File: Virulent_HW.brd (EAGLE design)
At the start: 52 parts, among them U1 STM32F050G6U6

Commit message: updated LED symbol
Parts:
- RGB1: value MSL0201RGBW15 -> MSL0201RGBLED
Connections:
- net +3.3V: now also RGB1.4; no longer RGB1.P$4
- net MOD_FREQ: now also U1.9
- net N$11: now also RGB1.1; no longer RGB1.P$1
- net N$15: now also RGB1.2; no longer RGB1.P$2
- net N$16: now also RGB1.3; no longer RGB1.P$3
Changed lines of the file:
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@@
 <element name="R9" library="Virulent_HW" package="R0402" value="10k" x="-33.02" y="-237.49"/>
 <element name="R10" library="Virulent_HW" package="R0402" value="10k" x="-33.02" y="-242.57"/>
-<element name="RGB1" library="Virulent_HW" package="MSL0201RGB" value="MSL0201RGBW15" x="-39.37" y="-241.3"/>
+<element name="RGB1" library="Virulent_HW" package="MSL0201RGB" value="MSL0201RGBLED" x="-39.37" y="-241.3"/>
 <element name="R11" library="Virulent_HW" package="R0402" value="10k" x="-40.64" y="-247.65"/>
 <element name="R12" library="Virulent_HW" package="R0402" value="10k" x="-40.64" y="-252.73"/>
@@
 <contactref element="R8" pad="2"/>
 <contactref element="R10" pad="2"/>
-<contactref element="RGB1" pad="P$4"/>
+<contactref element="RGB1" pad="4"/>
 <contactref element="R14" pad="2"/>
 <contactref element="R16" pad="2"/>
@@
 </signal>
 <signal name="N$11">
-<contactref element="RGB1" pad="P$1"/>
+<contactref element="RGB1" pad="1"/>
 <contactref element="R11" pad="1"/>
 <wire x1="-39.445" y1="-242.75" x2="-41.29" y2="-247.65" width="0" layer="19" extent="1-1"/>
 </signal>
 <signal name="N$15">
-<contactref element="RGB1" pad="P$2"/>
+<contactref element="RGB1" pad="2"/>
 <contactref element="R12" pad="1"/>
 <wire x1="-39.045" y1="-241.7" x2="-41.29" y2="-252.73" width="0" layer="19" extent="1-1"/>
 </signal>
 <signal name="N$16">
-<contactref element="RGB1" pad="P$3"/>
+<contactref element="RGB1" pad="3"/>
 <contactref element="R13" pad="1"/>
 <wire x1="-39.045" y1="-240.9" x2="-41.29" y2="-257.81" width="0" layer="19" extent="1-1"/>
@@
 <signal name="MOD_FREQ">
 <contactref element="SPST1" pad="4"/>
+<contactref element="U1" pad="9"/>
+<wire x1="-37.15" y1="-285.13" x2="-34.02" y2="-216.505" width="0" layer="19" extent="1-1"/>
 </signal>
 <signal name="N$26">

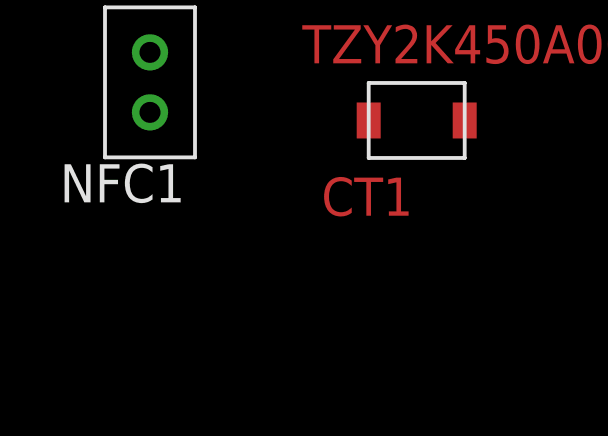
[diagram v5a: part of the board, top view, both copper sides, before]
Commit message: added no place capcitor to NFC coil transmitter in case needed
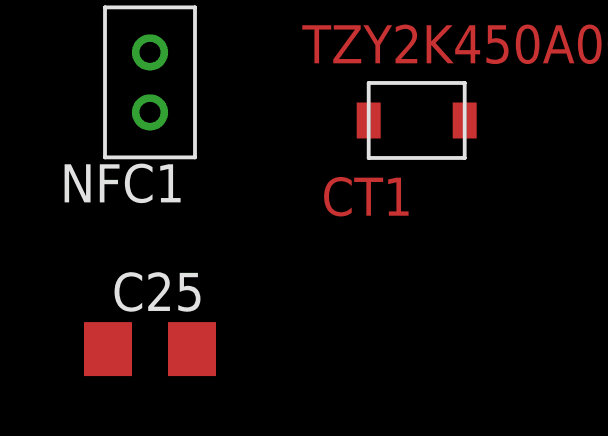
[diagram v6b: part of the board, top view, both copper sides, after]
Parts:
- added C25: NU, rcl:C1206
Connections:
- net GND: now also C25.2
- net N$26: now also C25.1
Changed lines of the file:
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@@
 <element name="CT1" library="Virulent_HW" package="TZY2" value="TZY2K450A001R002" x="-45.72" y="-292.1"/>
 <element name="NFC1" library="Virulent_HW" package="17M2-G" value="WR-383250-17M2-G" x="-54.61" y="-290.83"/>
+<element name="C25" library="rcl" package="C1206" value="NU" x="-54.61" y="-299.72"/>
 </elements>
 <signals>
@@
 <contactref element="SPST1" pad="3"/>
 <contactref element="CT1" pad="2"/>
+<contactref element="C25" pad="2"/>
 <wire x1="-26.54" y1="-215.9" x2="-31.145" y2="-215.63" width="0" layer="19" extent="1-1"/>
 <wire x1="-26.54" y1="-209.55" x2="-26.54" y2="-215.9" width="0" layer="19" extent="1-1"/>
@@
 <wire x1="-39.05" y1="-285.13" x2="-41.29" y2="-278.13" width="0" layer="19" extent="1-1"/>
 <wire x1="-44.12" y1="-292.1" x2="-39.05" y2="-285.13" width="0" layer="19" extent="1-1"/>
+<wire x1="-53.21" y1="-299.72" x2="-44.12" y2="-292.1" width="0" layer="19" extent="1-1"/>
 </signal>
 <signal name="5V_ENABLE">
@@
 <contactref element="NFC1" pad="2"/>
 <contactref element="CT1" pad="1"/>
+<contactref element="C25" pad="1"/>
+<wire x1="-54.61" y1="-291.83" x2="-56.01" y2="-299.72" width="0" layer="19" extent="1-1"/>
 <wire x1="-47.32" y1="-292.1" x2="-54.61" y2="-291.83" width="0" layer="19" extent="1-1"/>
 </signal>

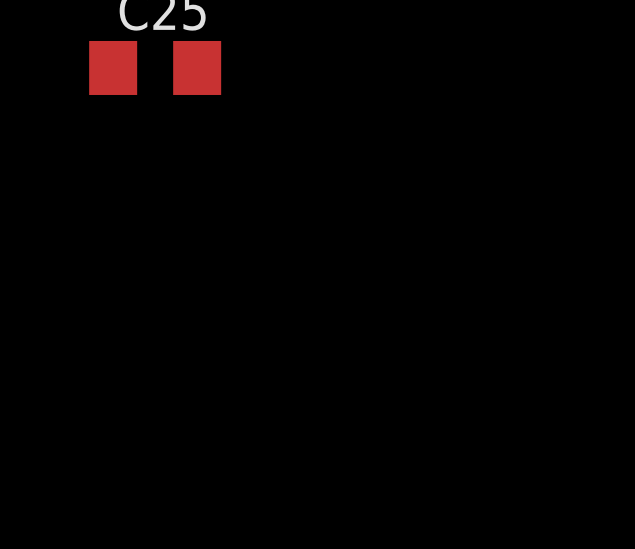
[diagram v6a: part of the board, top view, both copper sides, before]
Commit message: updated power symbol and a few revisions suggested by Andrew. Added team information.
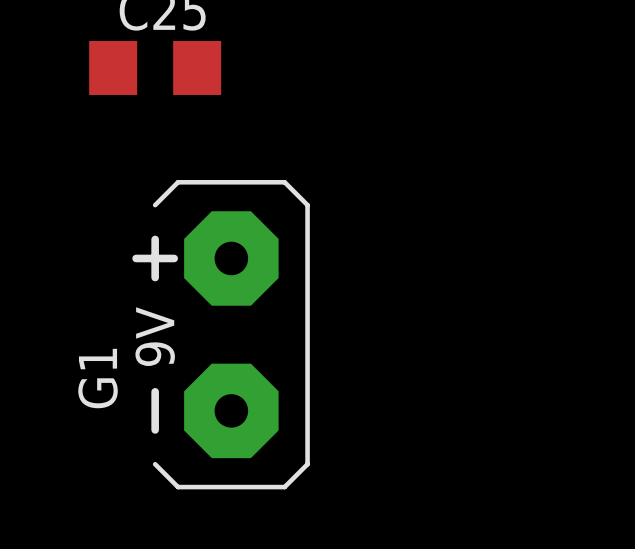
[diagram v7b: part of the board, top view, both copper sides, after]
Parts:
- added G1: AB9V, battery:AB9V
- C13: value 1n -> (none)
- C16, C20, C3: value 1u -> (none)
- C17: value 5.6n -> (none)
- C21: value 1.8n -> (none)
- R1: value 470k -> (none)
- R2: value 56k -> (none)
- R3: value 100k -> (none)
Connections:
- net +3.3V: no longer SPST1.5
- net +5V: now also SPST1.5
- net +9-36V: now also G1.+
- net GND: now also G1.-
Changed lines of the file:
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@@
 <element name="C1" library="rcl" package="C1206" value="" x="-19.05" y="-97.79"/>
 <element name="C2" library="rcl" package="C1206" value="" x="-19.05" y="-104.14"/>
-<element name="C3" library="rcl" package="C1206" value="1u" x="-19.05" y="-110.49"/>
-<element name="C13" library="rcl" package="C1206" value="1n" x="-19.05" y="-116.84"/>
-<element name="R1" library="Virulent_HW" package="R0402" value="470k" x="-20.32" y="-123.19"/>
+<element name="C3" library="rcl" package="C1206" value="" x="-19.05" y="-110.49"/>
+<element name="C13" library="rcl" package="C1206" value="" x="-19.05" y="-116.84"/>
+<element name="R1" library="Virulent_HW" package="R0402" value="" x="-20.32" y="-123.19"/>
 <element name="PLL2" library="Virulent_HW" package="SOIC-8" value="LM567CM/NOPB-ND" x="-17.78" y="-138.43"/>
 <element name="C14" library="rcl" package="C1206" value="" x="-8.89" y="-146.05"/>
 <element name="C15" library="rcl" package="C1206" value="" x="-19.05" y="-152.4"/>
-<element name="C16" library="rcl" package="C1206" value="1u" x="-10.16" y="-129.54"/>
-<element name="C17" library="rcl" package="C1206" value="5.6n" x="-19.05" y="-146.05"/>
-<element name="R2" library="Virulent_HW" package="R0402" value="56k" x="-13.97" y="-144.78"/>
+<element name="C16" library="rcl" package="C1206" value="" x="-10.16" y="-129.54"/>
+<element name="C17" library="rcl" package="C1206" value="" x="-19.05" y="-146.05"/>
+<element name="R2" library="Virulent_HW" package="R0402" value="" x="-13.97" y="-144.78"/>
 <element name="PLL3" library="Virulent_HW" package="SOIC-8" value="LM567CM/NOPB-ND" x="-17.78" y="-166.37"/>
 <element name="C18" library="rcl" package="C1206" value="" x="-8.89" y="-173.99"/>
 <element name="C19" library="rcl" package="C1206" value="" x="-19.05" y="-180.34"/>
-<element name="C20" library="rcl" package="C1206" value="1u" x="-10.16" y="-157.48"/>
-<element name="C21" library="rcl" package="C1206" value="1.8n" x="-19.05" y="-173.99"/>
-<element name="R3" library="Virulent_HW" package="R0402" value="100k" x="-13.97" y="-172.72"/>
+<element name="C20" library="rcl" package="C1206" value="" x="-10.16" y="-157.48"/>
+<element name="C21" library="rcl" package="C1206" value="" x="-19.05" y="-173.99"/>
+<element name="R3" library="Virulent_HW" package="R0402" value="" x="-13.97" y="-172.72"/>
 <element name="HEX1" library="Virulent_HW" package="TSSOP14" value="SN74ACT14PW" x="-17.78" y="-185.42"/>
 <element name="CTX1" library="Virulent_HW" package="4-SMD" value="405C11A13M5600\4-SMD" x="-26.67" y="-182.88"/>
@@
 <element name="NFC1" library="Virulent_HW" package="17M2-G" value="WR-383250-17M2-G" x="-54.61" y="-290.83"/>
 <element name="C25" library="rcl" package="C1206" value="NU" x="-54.61" y="-299.72"/>
+<element name="G1" library="battery" package="AB9V" value="AB9V" x="-52.07" y="-308.61"/>
 </elements>
 <signals>
@@
 <contactref element="R14" pad="2"/>
 <contactref element="R16" pad="2"/>
-<contactref element="SPST1" pad="5"/>
 <wire x1="-32.37" y1="-227.33" x2="-32.37" y2="-222.25" width="0" layer="19" extent="1-1"/>
 <wire x1="-32.37" y1="-232.41" x2="-32.37" y2="-227.33" width="0" layer="19" extent="1-1"/>
@@
 <wire x1="-39.99" y1="-262.89" x2="-32.37" y2="-242.57" width="0" layer="19" extent="1-1"/>
 <wire x1="-39.99" y1="-273.05" x2="-39.99" y2="-262.89" width="0" layer="19" extent="1-1"/>
-<wire x1="-37.15" y1="-283.83" x2="-39.99" y2="-273.05" width="0" layer="19" extent="1-1"/>
 <wire x1="-20.97" y1="-91.44" x2="-31.145" y2="-215.13" width="0" layer="19" extent="1-1"/>
 <wire x1="-20.97" y1="-87.63" x2="-20.97" y2="-91.44" width="0" layer="19" extent="1-1"/>
@@
 <contactref element="HEX1" pad="14"/>
 <contactref element="C24" pad="1"/>
+<contactref element="SPST1" pad="5"/>
 <wire x1="-20.055" y1="-182.495" x2="-29.34" y2="-215.9" width="0" layer="19" extent="1-1"/>
 <wire x1="-15.875" y1="-168.7195" x2="-20.055" y2="-182.495" width="0" layer="19" extent="1-1"/>
@@
 <wire x1="-16.637" y1="-48.26" x2="-20.97" y2="-58.42" width="0" layer="19" extent="1-1"/>
 <wire x1="-5.715" y1="-18.8595" x2="-16.637" y2="-48.26" width="0" layer="19" extent="1-1"/>
+<wire x1="-37.15" y1="-283.83" x2="-29.34" y2="-215.9" width="0" layer="19" extent="1-1"/>
 </signal>
 <signal name="+9-36V">
 <contactref element="VR1" pad="1"/>
 <contactref element="C4" pad="1"/>
+<contactref element="G1" pad="+"/>
+<wire x1="-20.45" y1="-54.61" x2="-52.07" y2="-306.07" width="0" layer="19" extent="1-1"/>
 <wire x1="-20.066" y1="-48.26" x2="-20.45" y2="-54.61" width="0" layer="19" extent="1-1"/>
 </signal>
@@
 <contactref element="R17" pad="1"/>
 <contactref element="SPST1" pad="3"/>
+<contactref element="C25" pad="2"/>
 <contactref element="CT1" pad="2"/>
-<contactref element="C25" pad="2"/>
+<contactref element="G1" pad="-"/>
 <wire x1="-26.54" y1="-215.9" x2="-31.145" y2="-215.63" width="0" layer="19" extent="1-1"/>
 <wire x1="-26.54" y1="-209.55" x2="-26.54" y2="-215.9" width="0" layer="19" extent="1-1"/>
@@
 <wire x1="-44.12" y1="-292.1" x2="-39.05" y2="-285.13" width="0" layer="19" extent="1-1"/>
 <wire x1="-53.21" y1="-299.72" x2="-44.12" y2="-292.1" width="0" layer="19" extent="1-1"/>
+<wire x1="-52.07" y1="-311.15" x2="-53.21" y2="-299.72" width="0" layer="19" extent="1-1"/>
 </signal>
 <signal name="5V_ENABLE">

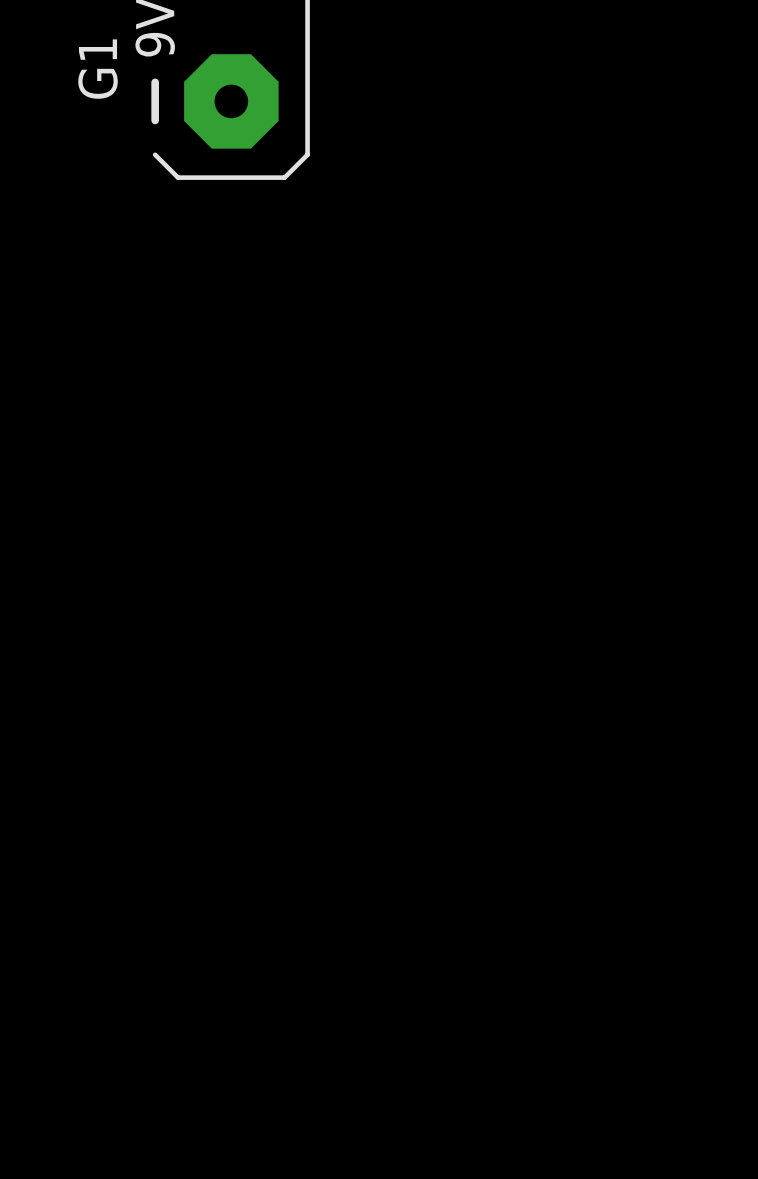
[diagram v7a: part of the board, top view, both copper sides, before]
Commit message: Added SWD connector, Bulk input capacitance.
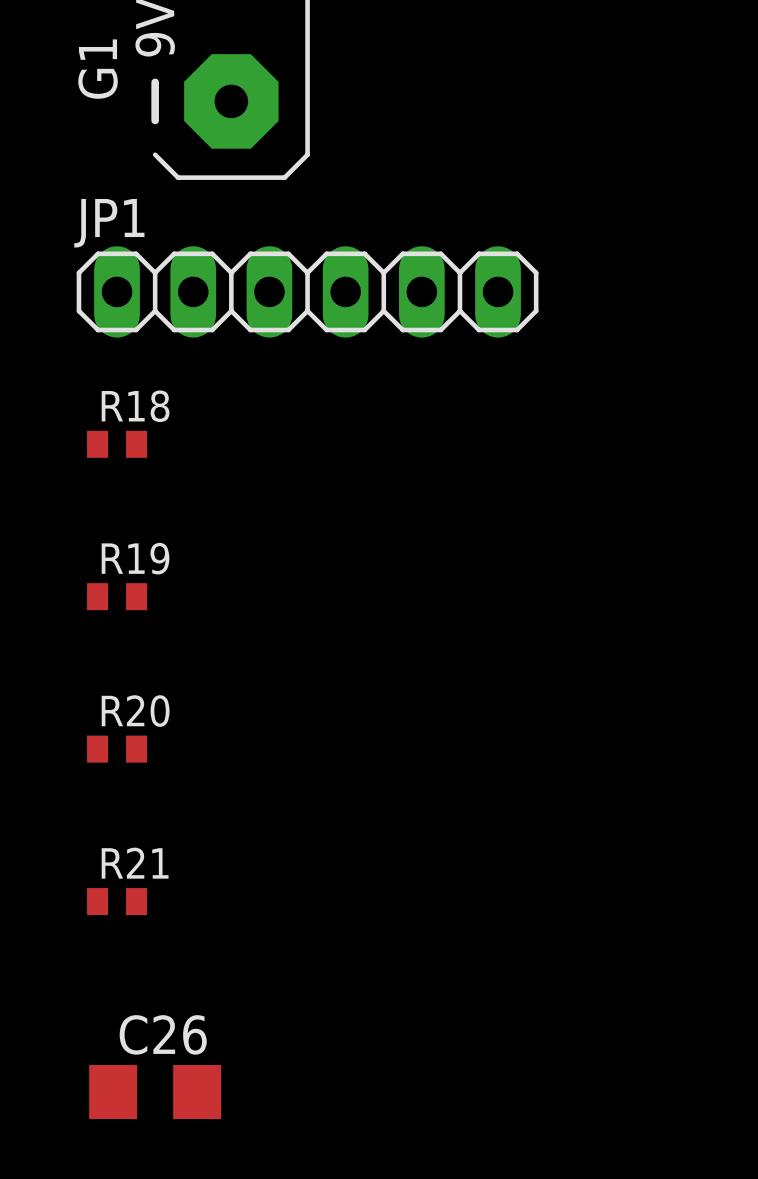
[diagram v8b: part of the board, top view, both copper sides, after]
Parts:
- added C26: 10u, rcl:C1206
- added JP1: (no value), Virulent_HW:1X06
- added R18, R20, R21: 22, Virulent_HW:R0402
- added R19: NU, Virulent_HW:R0402
- R11: value 10k -> 30
- R12: value 10k -> 120
- R13: value 10k -> 39.2
- R15, R17: value NU -> 10k
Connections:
- new net STM_SWCLK: R21.2, U1.22
- new net STM_SWDAT: R20.2, U1.21
- new net STM_SWO: R19.2, U1.23
- new net SWD_NRST: JP1.1, R18.1
- new net SWD_SWCLK: JP1.4, R21.1
- new net SWD_SWDAT: JP1.3, R20.1
- new net SWD_SWO: JP1.2, R19.1
- net +3.3V: now also JP1.6
- net +9-36V: now also C26.2
- net GND: now also C26.1, JP1.5
- net N$6: now also R18.2
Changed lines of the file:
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@@
 <element name="R10" library="Virulent_HW" package="R0402" value="10k" x="-33.02" y="-242.57"/>
 <element name="RGB1" library="Virulent_HW" package="MSL0201RGB" value="MSL0201RGBLED" x="-39.37" y="-241.3"/>
-<element name="R11" library="Virulent_HW" package="R0402" value="10k" x="-40.64" y="-247.65"/>
-<element name="R12" library="Virulent_HW" package="R0402" value="10k" x="-40.64" y="-252.73"/>
-<element name="R13" library="Virulent_HW" package="R0402" value="10k" x="-40.64" y="-257.81"/>
+<element name="R11" library="Virulent_HW" package="R0402" value="30" x="-40.64" y="-247.65"/>
+<element name="R12" library="Virulent_HW" package="R0402" value="120" x="-40.64" y="-252.73"/>
+<element name="R13" library="Virulent_HW" package="R0402" value="39.2" x="-40.64" y="-257.81"/>
 <element name="R14" library="Virulent_HW" package="R0402" value="NU" x="-40.64" y="-262.89"/>
-<element name="R15" library="Virulent_HW" package="R0402" value="NU" x="-40.64" y="-267.97"/>
+<element name="R15" library="Virulent_HW" package="R0402" value="10k" x="-40.64" y="-267.97"/>
 <element name="R16" library="Virulent_HW" package="R0402" value="NU" x="-40.64" y="-273.05"/>
-<element name="R17" library="Virulent_HW" package="R0402" value="NU" x="-40.64" y="-278.13"/>
+<element name="R17" library="Virulent_HW" package="R0402" value="10k" x="-40.64" y="-278.13"/>
 <element name="SPST1" library="Virulent_HW" package="6-TSSOP" value="FSA66SC70-5" x="-38.1" y="-284.48"/>
 <element name="CT1" library="Virulent_HW" package="TZY2" value="TZY2K450A001R002" x="-45.72" y="-292.1"/>
@@
 <element name="C25" library="rcl" package="C1206" value="NU" x="-54.61" y="-299.72"/>
 <element name="G1" library="battery" package="AB9V" value="AB9V" x="-52.07" y="-308.61"/>
+<element name="JP1" library="Virulent_HW" package="1X06" value="" x="-49.53" y="-317.5"/>
+<element name="R18" library="Virulent_HW" package="R0402" value="22" x="-55.88" y="-322.58"/>
+<element name="R19" library="Virulent_HW" package="R0402" value="NU" x="-55.88" y="-327.66"/>
+<element name="R20" library="Virulent_HW" package="R0402" value="22" x="-55.88" y="-332.74"/>
+<element name="R21" library="Virulent_HW" package="R0402" value="22" x="-55.88" y="-337.82"/>
+<element name="C26" library="rcl" package="C1206" value="10u" x="-54.61" y="-344.17"/>
 </elements>
 <signals>
@@
 <contactref element="R14" pad="2"/>
 <contactref element="R16" pad="2"/>
+<contactref element="JP1" pad="6"/>
 <wire x1="-32.37" y1="-227.33" x2="-32.37" y2="-222.25" width="0" layer="19" extent="1-1"/>
 <wire x1="-32.37" y1="-232.41" x2="-32.37" y2="-227.33" width="0" layer="19" extent="1-1"/>
@@
 <wire x1="-39.99" y1="-262.89" x2="-32.37" y2="-242.57" width="0" layer="19" extent="1-1"/>
 <wire x1="-39.99" y1="-273.05" x2="-39.99" y2="-262.89" width="0" layer="19" extent="1-1"/>
+<wire x1="-43.18" y1="-317.5" x2="-39.99" y2="-273.05" width="0" layer="19" extent="1-1"/>
 <wire x1="-20.97" y1="-91.44" x2="-31.145" y2="-215.13" width="0" layer="19" extent="1-1"/>
 <wire x1="-20.97" y1="-87.63" x2="-20.97" y2="-91.44" width="0" layer="19" extent="1-1"/>
@@
 <contactref element="C4" pad="1"/>
 <contactref element="G1" pad="+"/>
+<contactref element="C26" pad="2"/>
+<wire x1="-52.07" y1="-306.07" x2="-53.21" y2="-344.17" width="0" layer="19" extent="1-1"/>
 <wire x1="-20.45" y1="-54.61" x2="-52.07" y2="-306.07" width="0" layer="19" extent="1-1"/>
 <wire x1="-20.066" y1="-48.26" x2="-20.45" y2="-54.61" width="0" layer="19" extent="1-1"/>
@@
 <contactref element="CT1" pad="2"/>
 <contactref element="G1" pad="-"/>
+<contactref element="JP1" pad="5"/>
+<contactref element="C26" pad="1"/>
 <wire x1="-26.54" y1="-215.9" x2="-31.145" y2="-215.63" width="0" layer="19" extent="1-1"/>
 <wire x1="-26.54" y1="-209.55" x2="-26.54" y2="-215.9" width="0" layer="19" extent="1-1"/>
@@
 <wire x1="-53.21" y1="-299.72" x2="-44.12" y2="-292.1" width="0" layer="19" extent="1-1"/>
 <wire x1="-52.07" y1="-311.15" x2="-53.21" y2="-299.72" width="0" layer="19" extent="1-1"/>
+<wire x1="-45.72" y1="-317.5" x2="-52.07" y2="-311.15" width="0" layer="19" extent="1-1"/>
+<wire x1="-56.01" y1="-344.17" x2="-45.72" y2="-317.5" width="0" layer="19" extent="1-1"/>
 </signal>
 <signal name="5V_ENABLE">
@@
 <contactref element="U1" pad="4"/>
 <contactref element="R10" pad="1"/>
+<contactref element="R18" pad="2"/>
 <wire x1="-33.67" y1="-242.57" x2="-34.895" y2="-214.63" width="0" layer="19" extent="1-1"/>
+<wire x1="-55.23" y1="-322.58" x2="-33.67" y2="-242.57" width="0" layer="19" extent="1-1"/>
 </signal>
 <signal name="N$9">
@@
 <wire x1="-47.32" y1="-292.1" x2="-54.61" y2="-291.83" width="0" layer="19" extent="1-1"/>
 </signal>
+<signal name="SWD_NRST">
+<contactref element="JP1" pad="1"/>
+<contactref element="R18" pad="1"/>
+<wire x1="-55.88" y1="-317.5" x2="-56.53" y2="-322.58" width="0" layer="19" extent="1-1"/>
+</signal>
+<signal name="SWD_SWO">
+<contactref element="JP1" pad="2"/>
+<contactref element="R19" pad="1"/>
+<wire x1="-53.34" y1="-317.5" x2="-56.53" y2="-327.66" width="0" layer="19" extent="1-1"/>
+</signal>
+<signal name="SWD_SWDAT">
+<contactref element="JP1" pad="3"/>
+<contactref element="R20" pad="1"/>
+<wire x1="-50.8" y1="-317.5" x2="-56.53" y2="-332.74" width="0" layer="19" extent="1-1"/>
+</signal>
+<signal name="SWD_SWCLK">
+<contactref element="JP1" pad="4"/>
+<contactref element="R21" pad="1"/>
+<wire x1="-48.26" y1="-317.5" x2="-56.53" y2="-337.82" width="0" layer="19" extent="1-1"/>
+</signal>
+<signal name="STM_SWDAT">
+<contactref element="U1" pad="21"/>
+<contactref element="R20" pad="2"/>
+<wire x1="-55.23" y1="-332.74" x2="-31.045" y2="-213.13" width="0" layer="19" extent="1-1"/>
+</signal>
+<signal name="STM_SWCLK">
+<contactref element="U1" pad="22"/>
+<contactref element="R21" pad="2"/>
+<wire x1="-55.23" y1="-337.82" x2="-31.52" y2="-212.655" width="0" layer="19" extent="1-1"/>
+</signal>
+<signal name="STM_SWO">
+<contactref element="U1" pad="23"/>
+<contactref element="R19" pad="2"/>
+<wire x1="-55.23" y1="-327.66" x2="-32.02" y2="-212.755" width="0" layer="19" extent="1-1"/>
+</signal>
 </signals>
